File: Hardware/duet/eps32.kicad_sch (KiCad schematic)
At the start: 0 parts

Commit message: Adds ESP32 and pull up-down resistors
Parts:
- added C28: 100 nF, easyeda2kicad:C0402, symbol easyeda2kicad:CL05B104KO5NNNC
- added C29: CL05B104KO5NNNC, easyeda2kicad:C0402, symbol easyeda2kicad:CL05B104KO5NNNC
- added R11, R12, R13, R14, R18, R19, R20: 4.7k, easyeda2kicad:R0402, symbol easyeda2kicad:0402WGF4701TCE
- added R9: 10k, easyeda2kicad:R0402, symbol easyeda2kicad:0402WGF1002TCE
- added U9: ESP32-S3-WROOM-1, easyeda2kicad:WIRELM-SMD_ESP32-S3-WROOM-1, symbol easyeda2kicad:ESP32-S3-WROOM-1
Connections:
- new net +3.3V: C28.1, R12.2, R13.2, R14.2, R18.2, R19.2, R20.2, R9.2, U9.2 (3V3)
- new net ESP_EN: C29.1, R9.1, U9.3 (EN)
- new net FPGA-DONE: R20.1, U9.8 (IO15)
- new net FPGA-INITN: R19.1, U9.9 (IO16)
- new net FPGA-PROGRAMN: R18.1, U9.10 (IO17)
- new net FPGA-TCK: R11.1, U9.4 (IO4)
- new net FPGA-TDI: R12.1, U9.5 (IO5)
- new net FPGA-TDO: R14.1, U9.7 (IO7)
- new net FPGA-TMS: R13.1, U9.6 (IO6)
- new net GND: C28.2, C29.2, R11.2, U9.1 (GND), U9.40 (GND), U9.41 (GND)
- new net USB_D+: U9.14 (IO20)
- new net USB_D-: U9.13 (IO19)

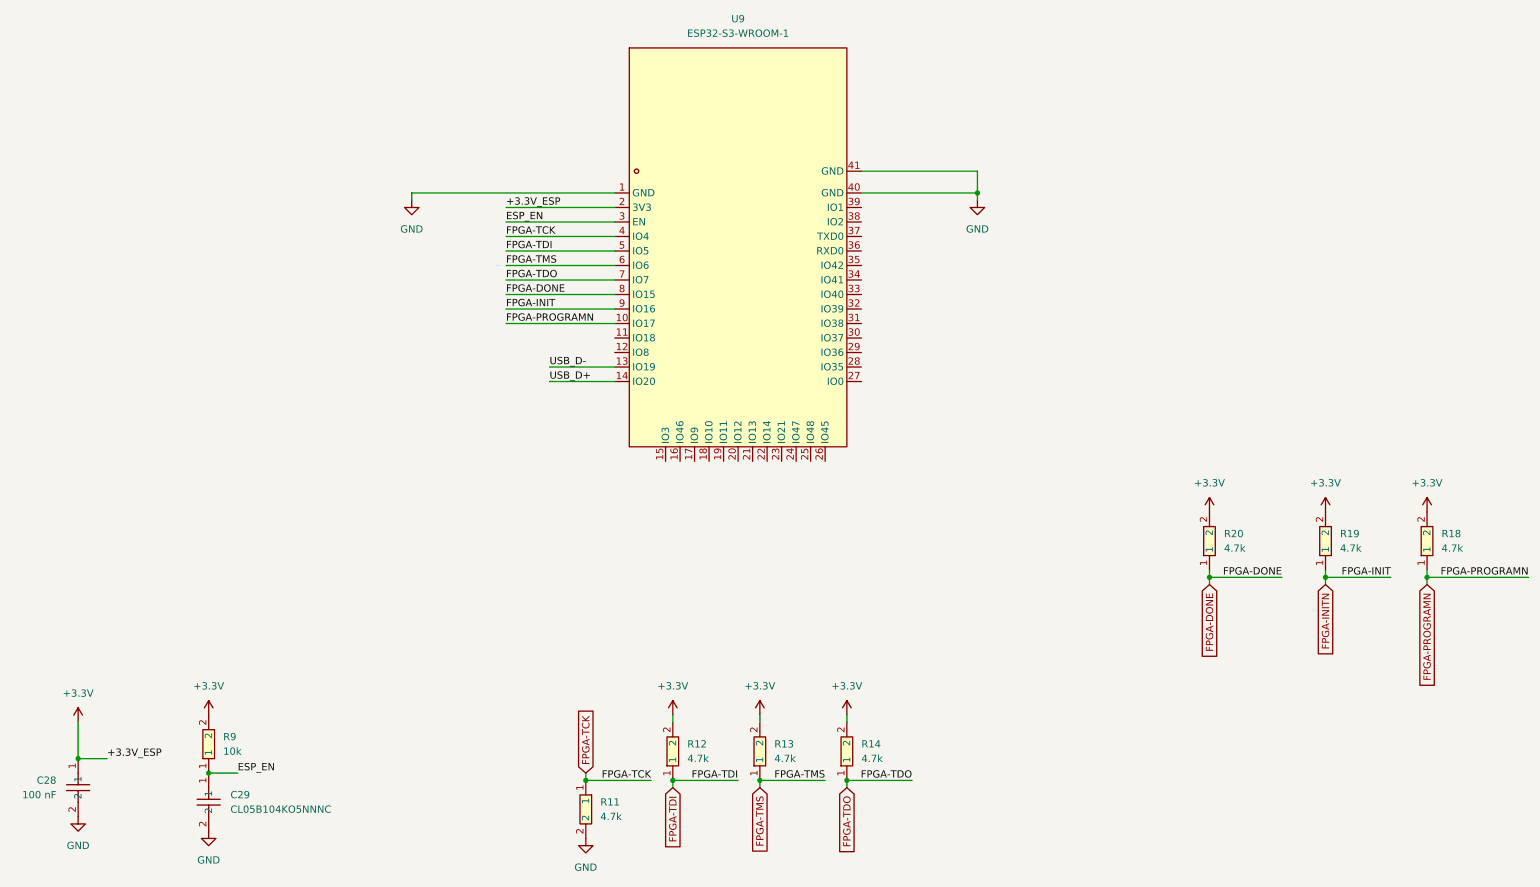
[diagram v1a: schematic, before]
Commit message: Add mezzanine connector and finalze HDMI
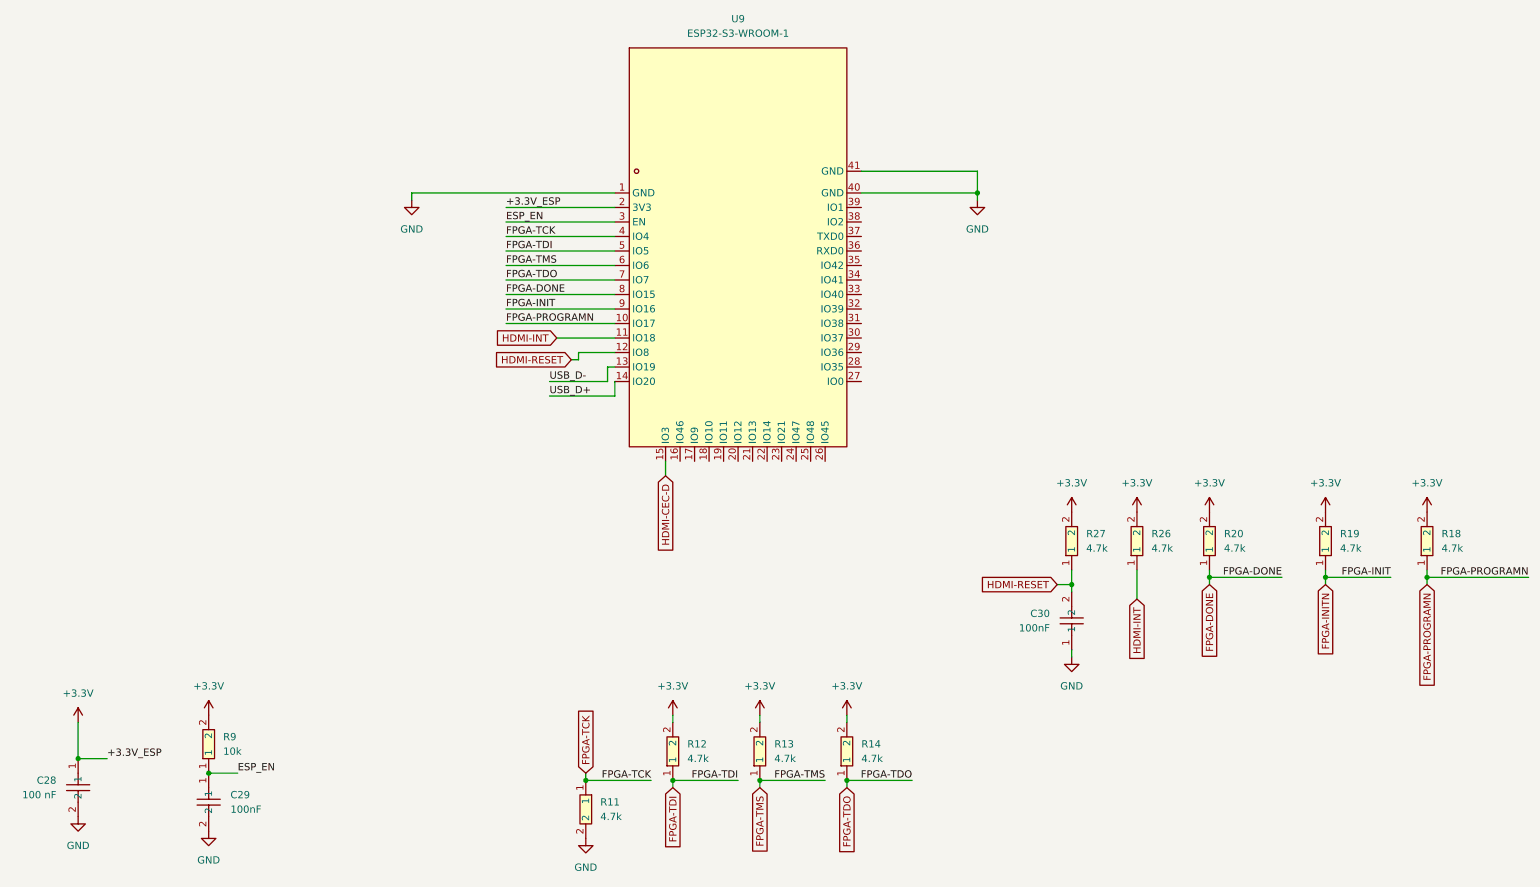
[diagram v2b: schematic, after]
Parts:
- added C30: 100nF, easyeda2kicad:C0402, symbol easyeda2kicad:CL05B104KO5NNNC
- added R26, R27: 4.7k, easyeda2kicad:R0402, symbol easyeda2kicad:0402WGF4701TCE
- C29: value CL05B104KO5NNNC -> 100nF
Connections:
- net +3.3V: now also R26.2, R27.2
- net GND: now also C30.1
- net HDMI-INT: now reaches U9.11 (IO18)
- net HDMI-INT: now also R26.1
- net HDMI-RESET: now reaches U9.12 (IO8)
- net HDMI-RESET: now also C30.2, R27.1
- net HDMI-CEC-D: now reaches U9.15 (IO3)
